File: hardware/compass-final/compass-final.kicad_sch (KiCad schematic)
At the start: 4 parts, among them U1 ESP32-DevKitC

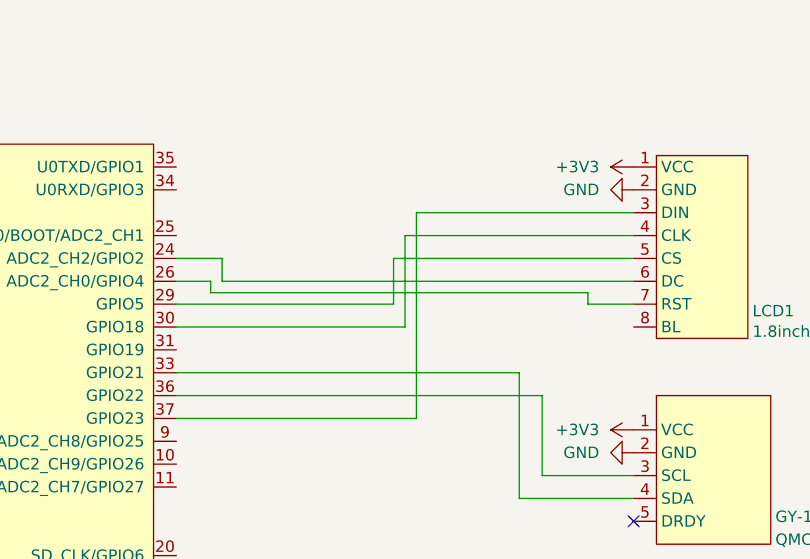
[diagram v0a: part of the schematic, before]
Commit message: Change display pins for assembly
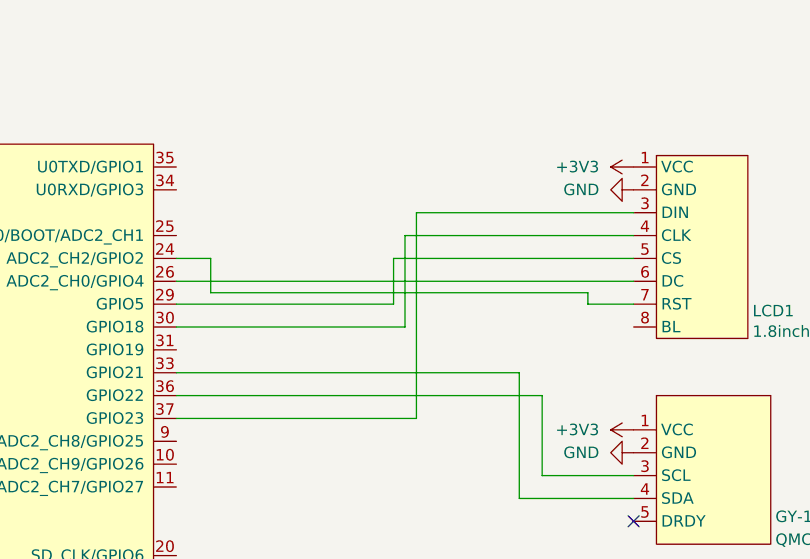
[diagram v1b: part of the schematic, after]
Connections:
- net at U1.24 (ADC2_CH2/GPIO2): now also LCD1.7 (RST); no longer LCD1.6 (DC)
- net at U1.26 (ADC2_CH0/GPIO4): now also LCD1.6 (DC); no longer LCD1.7 (RST)
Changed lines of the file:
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@@
-	(wire
-		(pts
-			(xy 134.62 73.66) (xy 130.81 73.66)
-		)
-		(stroke
-			(width 0)
-			(type default)
-		)
-	)
 	(wire
 		(pts
@@
 	(wire
 		(pts
-			(xy 135.89 71.12) (xy 130.81 71.12)
-		)
-		(stroke
-			(width 0)
-			(type default)
-		)
-	)
-	(wire
-		(pts
-			(xy 135.89 73.66) (xy 135.89 71.12)
-		)
-		(stroke
-			(width 0)
-			(type default)
-		)
-	)
-	(wire
-		(pts
 			(xy 168.91 83.82) (xy 168.91 97.79)
 		)
@@
 	(wire
 		(pts
-			(xy 181.61 73.66) (xy 135.89 73.66)
-		)
-		(stroke
-			(width 0)
-			(type default)
-		)
-	)
-	(wire
-		(pts
 			(xy 171.45 121.92) (xy 171.45 118.11)
 		)
@@
 	(wire
 		(pts
+			(xy 134.62 71.12) (xy 134.62 74.93)
+		)
+		(stroke
+			(width 0)
+			(type default)
+		)
+	)
+	(wire
+		(pts
 			(xy 181.61 68.58) (xy 156.21 68.58)
 		)
@@
 	(wire
 		(pts
+			(xy 134.62 71.12) (xy 130.81 71.12)
+		)
+		(stroke
+			(width 0)
+			(type default)
+		)
+	)
+	(wire
+		(pts
 			(xy 171.45 95.25) (xy 181.61 95.25)
 		)
@@
 	(wire
 		(pts
-			(xy 134.62 74.93) (xy 134.62 73.66)
-		)
-		(stroke
+			(xy 130.81 73.66) (xy 181.61 73.66)
+		)
+		(stroke
